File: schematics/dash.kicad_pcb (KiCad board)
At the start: 2 copper layers, 50 x 30 mm, 29 parts, among them J1 BATT_CONN, J2 EXTERNAL_TRIGGER, J3 USB_OTG, SW1 SW_Push, U1 ESP-12E, U2 ch340g, U3 MCP73833, U4 HT7333, Y1 12Mhz

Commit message: [add] Signature because fun
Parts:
- added G***: LOGO, LOGO, F.Cu at (137.2, 118.0)
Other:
- board text added: "tperale & carlos"
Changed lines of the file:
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@@
     (area 124.924999 94.924999 175.075001 125.075001)
     (thickness 1.6)
-    (drawings 10)
+    (drawings 11)
     (tracks 220)
     (zones 0)
-    (modules 29)
+    (modules 30)
     (nets 45)
   )
@@
     (add_net "Net-(U3-Pad9)")
   )
+  (module LOGO (layer F.Cu)
+    (at 137.25 118)
+    (fp_text reference G*** (at 0 0) (layer F.SilkS) hide
+      (effects (font (thickness 0.3)))
+    )
+    (fp_text value LOGO (at 0.75 0) (layer F.SilkS) hide
+      (effects (font (thickness 0.3)))
+    )
+    (fp_poly (pts (xy 3.386667 2.54) (xy -3.386666 2.54) (xy -3.386666 -0.016933) (xy -2.985911 -0.016933)
+      (xy -2.985911 1.619956) (xy -2.415822 1.619956) (xy -2.415822 0.564445) (xy -1.924813 0.564445)
+      (xy -1.923373 1.093611) (xy -1.921933 1.622778) (xy -1.365955 1.625706) (xy -1.365955 2.178756)
+      (xy -0.231422 2.178756) (xy -0.231422 1.603022) (xy -1.337851 1.603022) (xy -1.336381 1.353256)
+      (xy -1.334911 1.103489) (xy 1.312334 1.103489) (xy 1.315276 1.591733) (xy 0.248356 1.591733)
+      (xy 0.248356 1.876316) (xy 0.248422 1.932162) (xy 0.248612 1.984728) (xy 0.248913 2.032907)
+      (xy 0.249313 2.075588) (xy 0.249797 2.111663) (xy 0.250353 2.140022) (xy 0.250969 2.159556)
+      (xy 0.25163 2.169156) (xy 0.251782 2.169827) (xy 0.253145 2.171314) (xy 0.25646 2.172628)
+      (xy 0.262378 2.173779) (xy 0.271551 2.174779) (xy 0.28463 2.175637) (xy 0.302267 2.176364)
+      (xy 0.325114 2.176971) (xy 0.353822 2.177468) (xy 0.389043 2.177866) (xy 0.431429 2.178174)
+      (xy 0.481631 2.178405) (xy 0.540301 2.178568) (xy 0.608091 2.178673) (xy 0.685653 2.178732)
+      (xy 0.773637 2.178754) (xy 0.804937 2.178756) (xy 1.354667 2.178756) (xy 1.354667 1.614311)
+      (xy 1.9304 1.614311) (xy 1.9304 0.564322) (xy 2.168878 0.565794) (xy 2.407356 0.567267)
+      (xy 2.407356 1.625601) (xy 2.696634 1.625601) (xy 2.985911 1.6256) (xy 2.985911 -0.045155)
+      (xy 2.444158 -0.045155) (xy 2.44269 -0.303389) (xy 2.441222 -0.561622) (xy 2.174522 -0.563089)
+      (xy 1.907822 -0.564555) (xy 1.907822 -1.106311) (xy 1.326445 -1.106311) (xy 1.326445 -1.6256)
+      (xy 1.919111 -1.6256) (xy 1.919111 -2.173111) (xy 1.315156 -2.173111) (xy 1.315156 -1.636889)
+      (xy 0.784692 -1.636889) (xy 0.783224 -1.378655) (xy 0.781756 -1.120422) (xy -0.798689 -1.120422)
+      (xy -0.799741 -1.377244) (xy -0.800793 -1.634067) (xy -1.332089 -1.636999) (xy -1.332089 -2.150533)
+      (xy -1.901963 -2.150533) (xy -1.905049 -2.137833) (xy -1.905663 -2.129643) (xy -1.906166 -2.111391)
+      (xy -1.90655 -2.084302) (xy -1.906807 -2.049603) (xy -1.90693 -2.008519) (xy -1.906913 -1.962277)
+      (xy -1.906747 -1.912103) (xy -1.906567 -1.8796) (xy -1.905 -1.634067) (xy -1.62131 -1.632603)
+      (xy -1.337619 -1.63114) (xy -1.340555 -1.114778) (xy -1.627011 -1.113315) (xy -1.913466 -1.111852)
+      (xy -1.913466 -0.547623) (xy -2.441222 -0.544689) (xy -2.444156 -0.016933) (xy -2.985911 -0.016933)
+      (xy -3.386666 -0.016933) (xy -3.386666 -2.534355) (xy 3.386667 -2.534355) (xy 3.386667 2.54)) (layer F.SilkS) (width 0.01))
+    (fp_poly (pts (xy -0.824089 -0.005644) (xy -1.354777 -0.005644) (xy -1.353311 -0.272344) (xy -1.351844 -0.539044)
+      (xy -1.087966 -0.540683) (xy -0.824089 -0.542321) (xy -0.824089 -0.005644)) (layer F.SilkS) (width 0.01))
+    (fp_poly (pts (xy 1.319445 -0.272344) (xy 1.317978 -0.008467) (xy 1.057919 -0.007) (xy 1.004787 -0.006781)
+      (xy 0.955141 -0.006733) (xy 0.910116 -0.006844) (xy 0.870847 -0.007106) (xy 0.838468 -0.007508)
+      (xy 0.814116 -0.00804) (xy 0.798925 -0.008692) (xy 0.794041 -0.009352) (xy 0.793264 -0.015605)
+      (xy 0.79254 -0.032016) (xy 0.791886 -0.057452) (xy 0.791317 -0.090781) (xy 0.79085 -0.130871)
+      (xy 0.790501 -0.176591) (xy 0.790287 -0.226808) (xy 0.790222 -0.274696) (xy 0.790222 -0.536222)
+      (xy 1.320912 -0.536222) (xy 1.319445 -0.272344)) (layer F.SilkS) (width 0.01))
+  )
   (module TO_SOT_Packages_SMD:SOT89-3_Housing_Handsoldering (layer B.Cu)
     (at 152.75 98.25 90)
@@
     )
   )
+  (gr_text "tperale & carlos" (at 138 121.75) (layer F.SilkS)
+    (effects (font (size 1.5 1.5) (thickness 0.3)))
+  )
+  (gr_arc (start 130 120) (end 130 125) (angle 90) (layer Edge.Cuts) (width 0.15))
   (gr_line (start 171 125) (end 172 125) (angle 90) (layer Edge.Cuts) (width 0.15))
   (gr_line (start 175 120) (end 175 122) (angle 90) (layer Edge.Cuts) (width 0.15))
@@
   (gr_arc (start 170 100) (end 170 95) (angle 90) (layer Edge.Cuts) (width 0.15))
   (gr_arc (start 130 100) (end 125 100) (angle 90) (layer Edge.Cuts) (width 0.15))
-  (gr_arc (start 130 120) (end 130 125) (angle 90) (layer Edge.Cuts) (width 0.15))
   (gr_line (start 125 100) (end 125 120) (angle 90) (layer Edge.Cuts) (width 0.15))
   (gr_line (start 170 95) (end 130 95) (angle 90) (layer Edge.Cuts) (width 0.15))

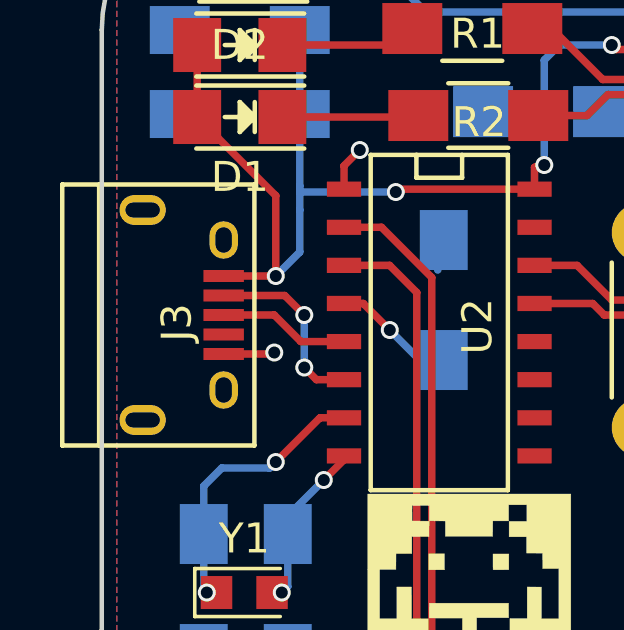
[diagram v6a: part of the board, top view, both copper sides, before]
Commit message: [fix] Fill the zone correctly
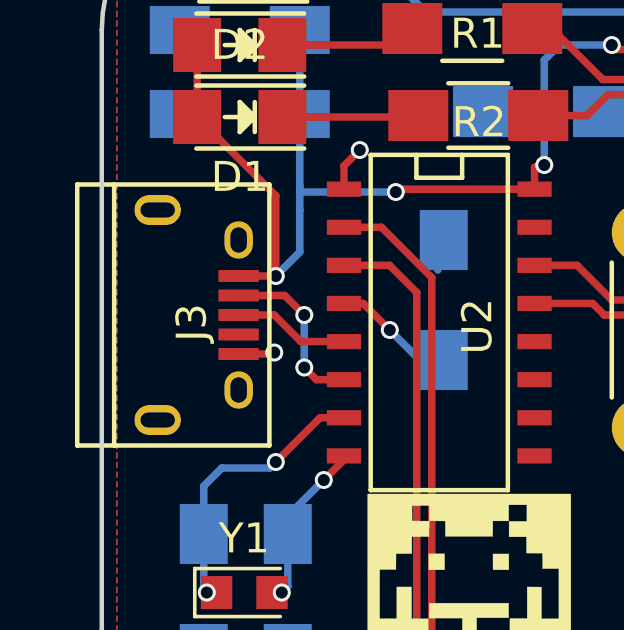
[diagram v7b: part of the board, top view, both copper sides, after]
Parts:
- moved J3 0.50 mm to (128.0, 109.5)
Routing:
- net GND: track 22.3 -> 21.8 mm
- net /D-: track 6.20 -> 5.70 mm
- net /D+: track 4.38 -> 3.88 mm
- net +5V: track 36.1 -> 35.6 mm
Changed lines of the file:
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@@
   )
   (module Connect:USB_Micro-B (layer F.Cu)
-    (at 127.5 109.5 270)
+    (at 128 109.5 270)
     (descr "Micro USB Type B Receptacle")
     (tags "USB USB_B USB_micro USB_OTG")
@@
   (segment (start 144.25 117) (end 144.25 114.5) (width 0.25) (layer F.Cu) (net 2) (status 10))
   (segment (start 144.25 114.5) (end 143 113.25) (width 0.25) (layer F.Cu) (net 2))
-  (segment (start 129.06254 110.7991) (end 130.7009 110.7991) (width 0.25) (layer F.Cu) (net 2))
+  (segment (start 129.56254 110.7991) (end 130.7009 110.7991) (width 0.25) (layer F.Cu) (net 2) (status 10))
   (via (at 130.75 110.75) (size 0.6) (drill 0.4) (layers F.Cu B.Cu) (net 2))
   (segment (start 130.7009 110.7991) (end 130.75 110.75) (width 0.25) (layer F.Cu) (net 2))
@@
   (segment (start 146.79 117) (end 146.79 113.96) (width 0.25) (layer F.Cu) (net 10) (status 10))
   (segment (start 146.79 113.96) (end 147.5 113.25) (width 0.25) (layer F.Cu) (net 10))
-  (segment (start 129.06254 108.8491) (end 131.0991 108.8491) (width 0.25) (layer F.Cu) (net 11))
+  (segment (start 129.56254 108.8491) (end 131.0991 108.8491) (width 0.25) (layer F.Cu) (net 11) (status 10))
   (segment (start 132.155 111.655) (end 133.075 111.655) (width 0.25) (layer F.Cu) (net 11))
   (segment (start 131.75 111.25) (end 132.155 111.655) (width 0.25) (layer F.Cu) (net 11))
@@
   (via (at 131.75 109.5) (size 0.6) (drill 0.4) (layers F.Cu B.Cu) (net 11))
   (segment (start 131.0991 108.8491) (end 131.75 109.5) (width 0.25) (layer F.Cu) (net 11))
-  (segment (start 129.06254 109.4991) (end 130.7491 109.4991) (width 0.25) (layer F.Cu) (net 12))
+  (segment (start 129.56254 109.4991) (end 130.7491 109.4991) (width 0.25) (layer F.Cu) (net 12) (status 10))
   (segment (start 131.635 110.385) (end 133.075 110.385) (width 0.25) (layer F.Cu) (net 12))
   (segment (start 130.7491 109.4991) (end 131.635 110.385) (width 0.25) (layer F.Cu) (net 12))
@@
   (segment (start 134.8 105.4) (end 134.895 105.305) (width 0.25) (layer F.Cu) (net 35))
   (via (at 134.8 105.4) (size 0.6) (drill 0.4) (layers F.Cu B.Cu) (net 35))
-  (segment (start 129.06254 108.1991) (end 130.7991 108.1991) (width 0.25) (layer F.Cu) (net 35))
+  (segment (start 129.56254 108.1991) (end 130.7991 108.1991) (width 0.25) (layer F.Cu) (net 35) (status 10))
   (segment (start 131.6 107.4) (end 131.6 106) (width 0.25) (layer B.Cu) (net 35))
   (segment (start 131.6 106) (end 131.6 105.4) (width 0.25) (layer B.Cu) (net 35))

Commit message: [fix] upgrade components to match our needs
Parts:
- C1: footprint Capacitors_SMD:C_1206_HandSoldering -> Capacitors_Tantalum_SMD:CP_Tantalum_Case-D_EIA-7343-31_Hand
- C7: footprint Capacitors_Tantalum_SMD:Tantalum_Case-A_EIA-3216-18_Hand -> Capacitors_Tantalum_SMD:CP_Tantalum_Case-A_EIA-3216-18_Hand
- C9: footprint Capacitors_Tantalum_SMD:Tantalum_Case-D_EIA-7343-31_Hand -> Capacitors_Tantalum_SMD:CP_Tantalum_Case-D_EIA-7343-31_Hand
- J1: footprint Pin_Headers:Pin_Header_Angled_1x02 -> Connectors_JST:JST_GH_SM02B-GHS-TB_02x1.25mm_Angled
- J2: footprint Pin_Headers:Pin_Header_Straight_1x02 -> Connectors_JST:JST_GH_BM02B-GHS-TBT_02x1.25mm_Straight
- J3: footprint Connect:USB_Micro-B -> Connectors:USB_Micro-B
- SW1: footprint Buttons_Switches_ThroughHole:SW_PUSH_6mm -> Buttons_Switches_THT:SW_PUSH_6mm
- Y1: footprint Crystals:Crystal_SMD_2012-2pin_2.0x1.2mm_HandSoldering -> Crystals:Crystal_SMD_3225-4pin_3.2x2.5mm_HandSoldering
- moved J1 6.30 mm to (170.8, 110.5), turned to 270 degrees
- moved J2 1.68 mm to (145.0, 118.5), turned to 180 degrees
- moved Y1 1.46 mm to (128.5, 118.0), turned to 270 degrees
- moved C7 0.28 mm to (158.8, 109.2)
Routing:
- net Net-(J3-Pad6): track 0.00 -> 13.9 mm
- net /WAKE: track 38.7 -> 46.8 mm
- net Net-(C3-Pad1): track 5.89 -> 10.9 mm
- net Net-(C1-Pad1): track 32.0 -> 35.3 mm
- net GND: track 21.8 -> 22.5 mm, vias 5 -> 6
